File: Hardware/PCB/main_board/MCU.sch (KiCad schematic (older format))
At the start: 1 part, among them U2 NUCLEO-F446RE

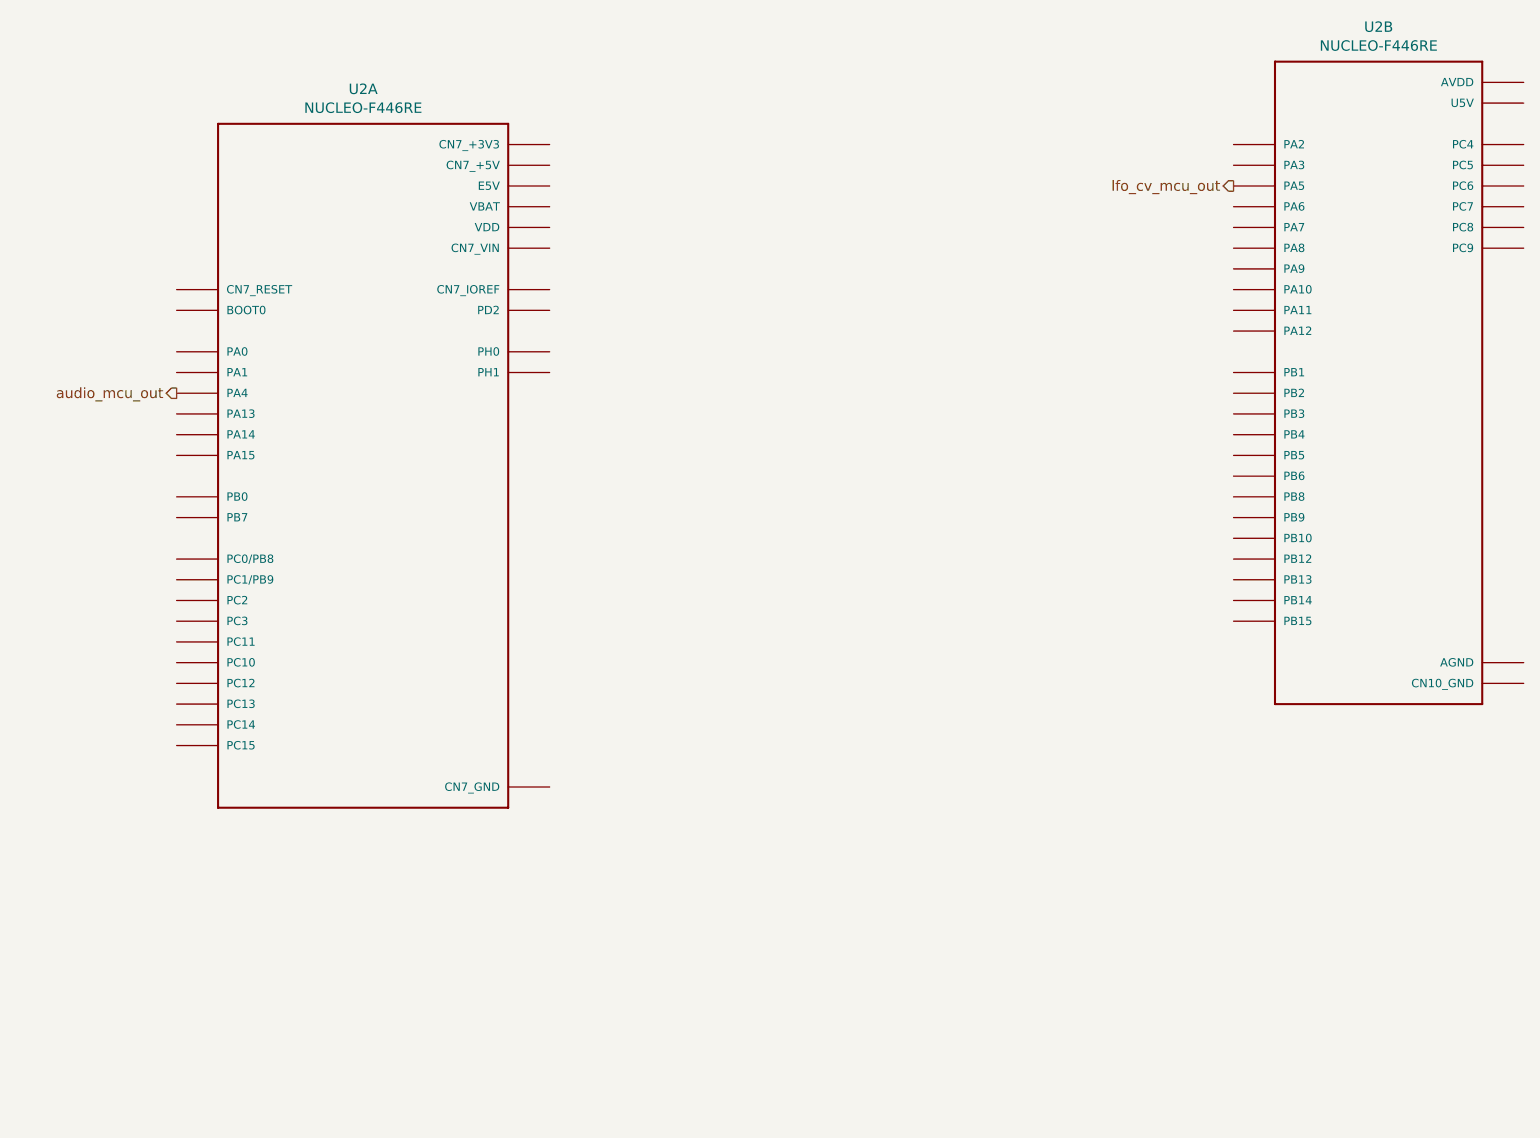
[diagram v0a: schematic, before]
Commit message: Add programming connector to PCB
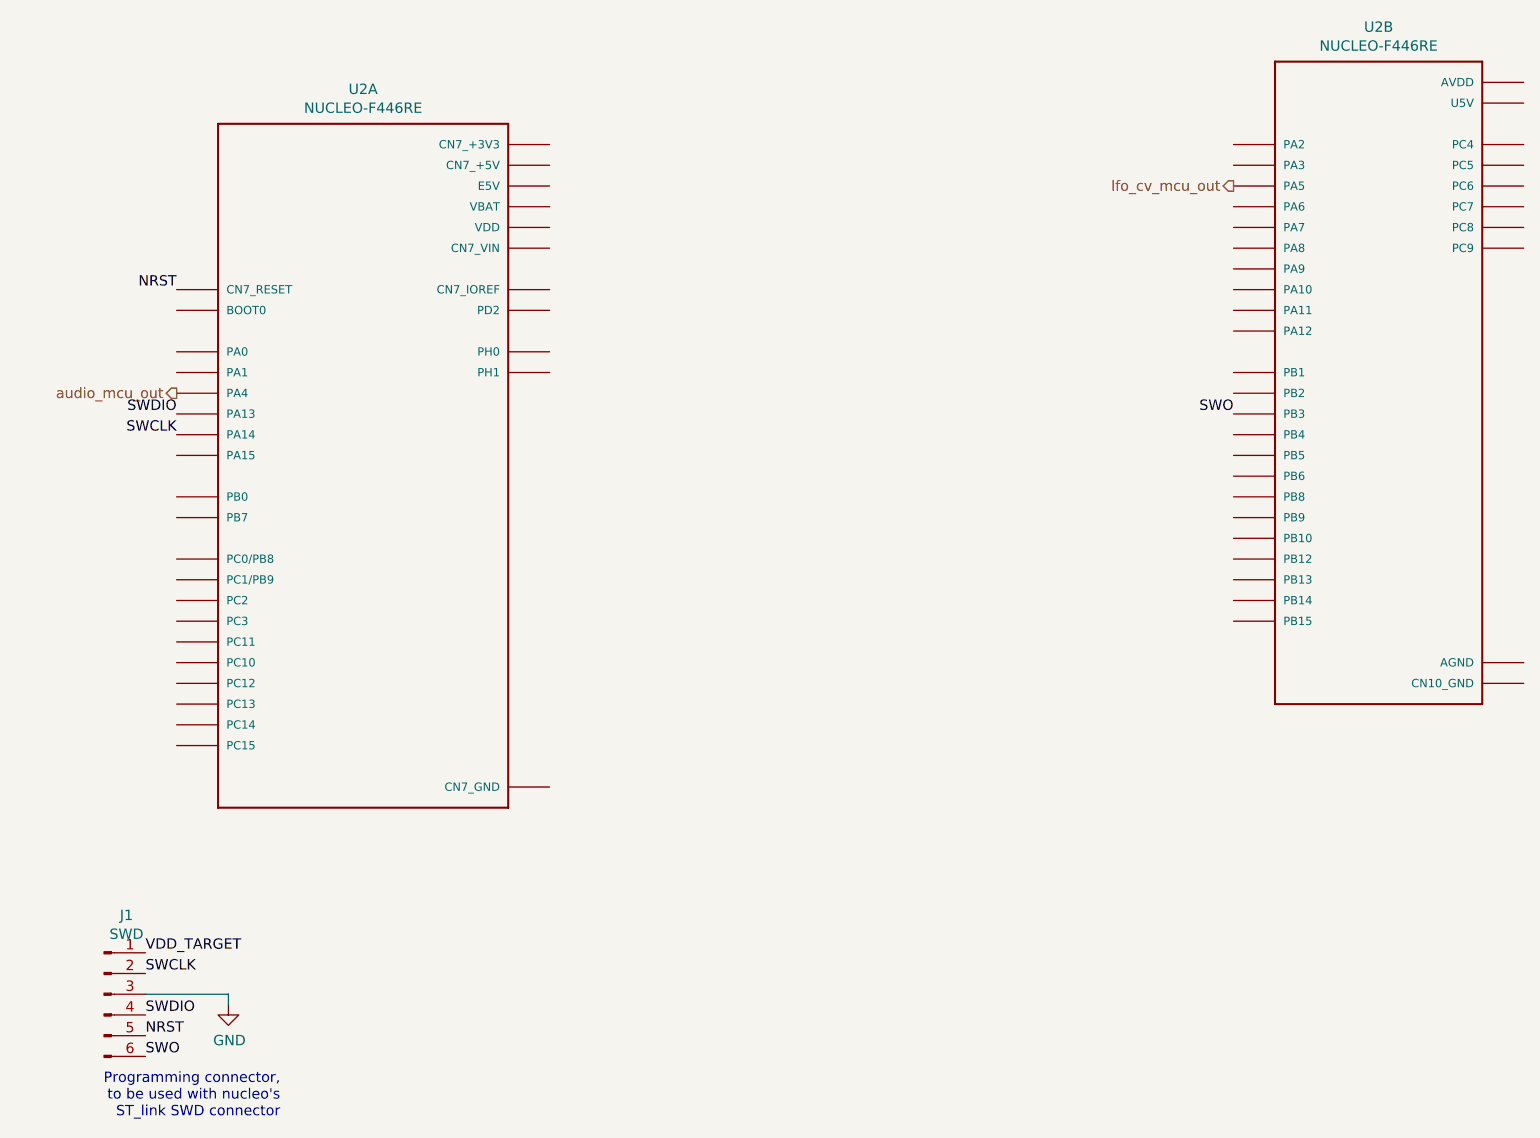
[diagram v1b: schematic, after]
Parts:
- added J1: SWD, Connector_PinHeader_1.27mm:PinHeader_1x06_P1.27mm_Vertical, symbol Connector:Conn_01x06_Male
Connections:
- net SWDIO: now reaches U2.CN7_13 (PA13)
- net SWDIO: now also J1.4 (Pin_4)
- net NRST: now reaches U2.CN7_14 (CN7_RESET)
- net NRST: now also J1.5 (Pin_5)
- net SWCLK: now reaches U2.CN7_15 (PA14)
- net SWCLK: now also J1.2 (Pin_2)
- net SWO: now reaches U2.CN10_31 (PB3)
- net SWO: now also J1.6 (Pin_6)
- new net GND: J1.3 (Pin_3)
- new net VDD_TARGET: J1.1 (Pin_1)
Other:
- note added: "Programming connector,\nto be used with nucleo's\nST_link SWD connector"
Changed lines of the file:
@@
 Text HLabel 7650 2250 0    50   Output ~ 0
 lfo_cv_mcu_out
+$Comp
+L Connector:Conn_01x06_Male J1
+U 1 1 5E51B937
+P 2200 6150
+F 0 "J1" H 2308 6531 50  0000 C CNN
+F 1 "SWD" H 2308 6440 50  0000 C CNN
+F 2 "Connector_PinHeader_1.27mm:PinHeader_1x06_P1.27mm_Vertical" H 2200 6150 50  0001 C CNN
+F 3 "~" H 2200 6150 50  0001 C CNN
+	1    2200 6150
+	1    0    0    -1
+$EndComp
+Text Label 2400 5950 0    50   ~ 0
+VDD_TARGET
+Text Label 2400 6050 0    50   ~ 0
+SWCLK
+Text Label 2400 6250 0    50   ~ 0
+SWDIO
+Text Label 2400 6350 0    50   ~ 0
+NRST
+Text Label 2400 6450 0    50   ~ 0
+SWO
+$Comp
+L power:GND #PWR0102
+U 1 1 5E51E3F2
+P 2800 6200
+F 0 "#PWR0102" H 2800 5950 50  0001 C CNN
+F 1 "GND" H 2805 6027 50  0000 C CNN
+F 2 "" H 2800 6200 50  0001 C CNN
+F 3 "" H 2800 6200 50  0001 C CNN
+	1    2800 6200
+	1    0    0    -1
+$EndComp
+Wire Wire Line
+	2400 6150 2800 6150
+Wire Wire Line
+	2800 6150 2800 6200
+Text Label 2550 3450 2    50   ~ 0
+SWCLK
+Text Label 2550 3350 2    50   ~ 0
+SWDIO
+Text Label 2550 2750 2    50   ~ 0
+NRST
+Text Label 7650 3350 2    50   ~ 0
+SWO
+Text Notes 3050 6750 2    50   ~ 0
+Programming connector,\nto be used with nucleo's\nST_link SWD connector
 $EndSCHEMATC

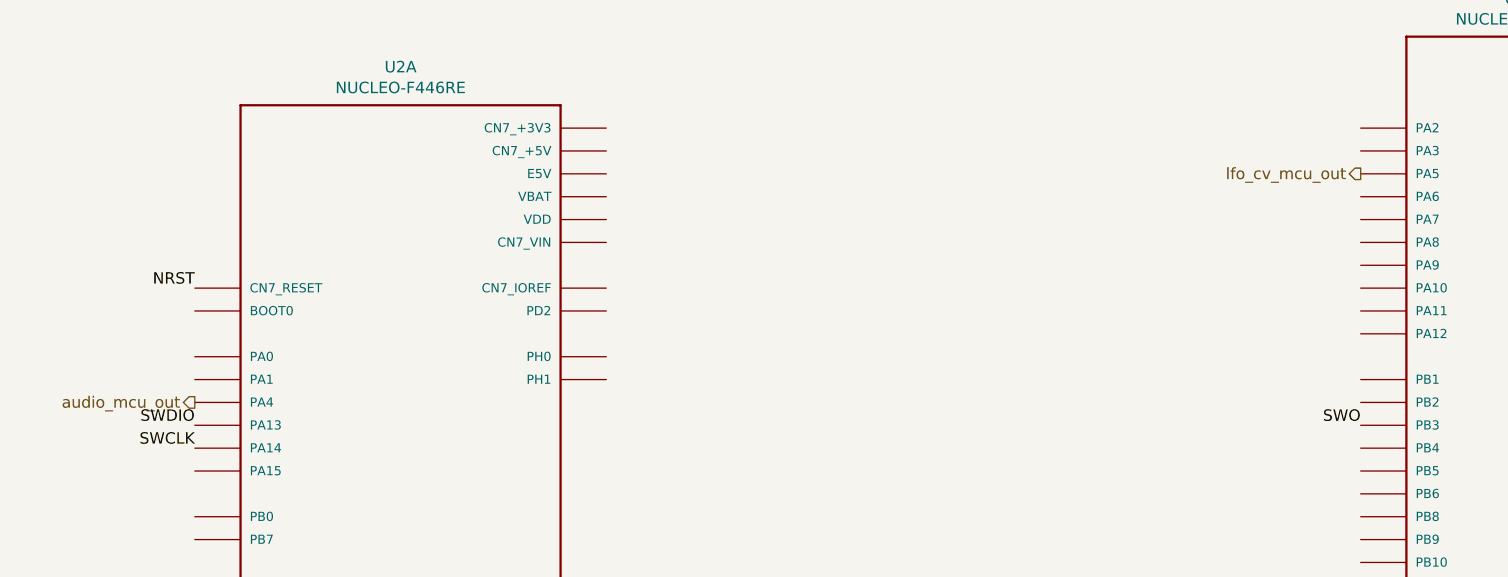
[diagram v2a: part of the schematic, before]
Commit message: Add power supply schematics and layout
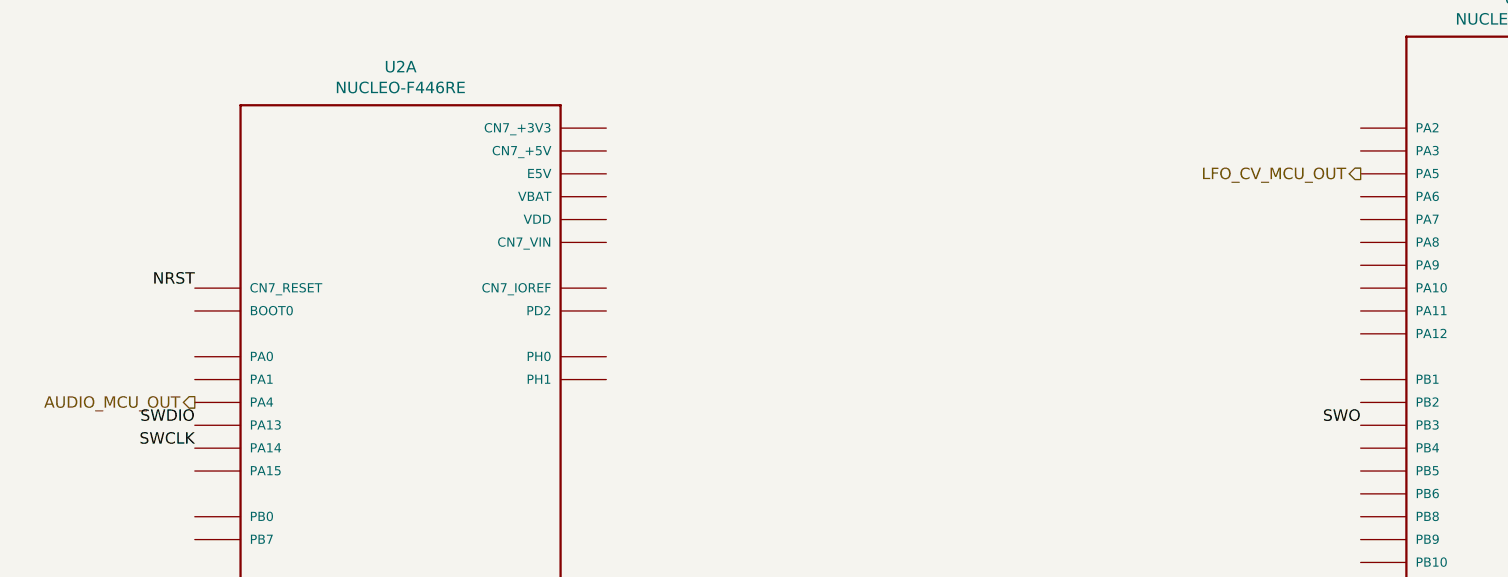
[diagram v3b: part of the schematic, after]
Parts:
- U2: footprint MODULE_NUCLEO-F446RE -> lib:MODULE_NUCLEO-F446RE
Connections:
- net audio_mcu_out renamed AUDIO_MCU_OUT
- net lfo_cv_mcu_out renamed LFO_CV_MCU_OUT
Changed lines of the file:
@@
 $Descr A4 11693 8268
 encoding utf-8
-Sheet 3 4
+Sheet 4 5
 Title ""
 Date ""
@@
 F 0 "U2" H 3450 5317 50  0000 C CNN
 F 1 "NUCLEO-F446RE" H 3450 5226 50  0000 C CNN
-F 2 "MODULE_NUCLEO-F446RE" H 3450 3550 50  0001 L BNN
+F 2 "lib:MODULE_NUCLEO-F446RE" H 3450 3550 50  0001 L BNN
 F 3 "" H 3450 3550 50  0001 L BNN
 F 4 "STMicroelectronics" H 3450 3550 50  0001 L BNN "Champ4"
@@
 F 0 "U2" H 8350 4817 50  0000 C CNN
 F 1 "NUCLEO-F446RE" H 8350 4726 50  0000 C CNN
-F 2 "MODULE_NUCLEO-F446RE" H 8350 3150 50  0001 L BNN
+F 2 "lib:MODULE_NUCLEO-F446RE" H 8350 3150 50  0001 L BNN
 F 3 "" H 8350 3150 50  0001 L BNN
 F 4 "STMicroelectronics" H 8350 3150 50  0001 L BNN "Champ4"
@@
 $EndComp
 Text HLabel 2550 3250 0    50   Output ~ 0
-audio_mcu_out
+AUDIO_MCU_OUT
 Text HLabel 7650 2250 0    50   Output ~ 0
-lfo_cv_mcu_out
+LFO_CV_MCU_OUT
 $Comp
 L Connector:Conn_01x06_Male J1

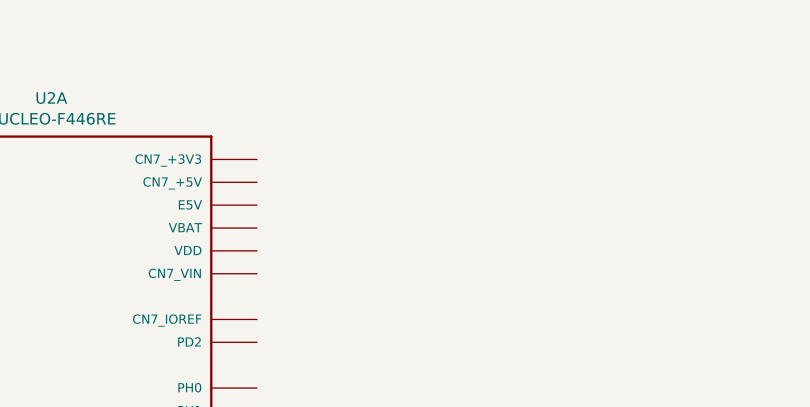
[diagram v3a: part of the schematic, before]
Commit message: Add missing power connection
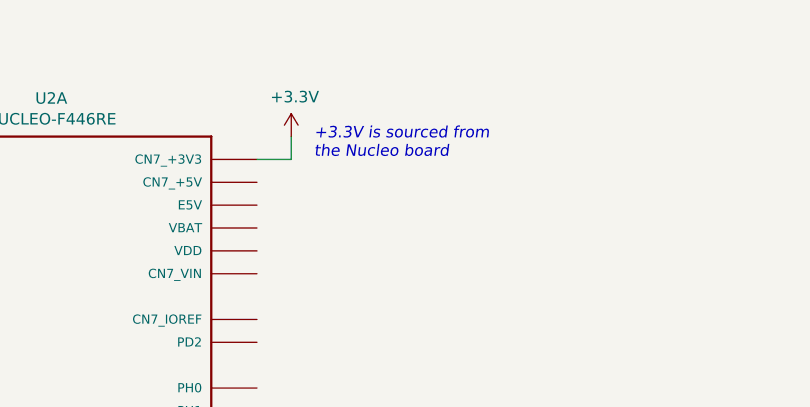
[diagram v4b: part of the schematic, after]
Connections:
- net +3V3: now reaches U2.CN7_16 (CN7_+3V3)
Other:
- note added: "+3.3V is sourced from\nthe Nucleo board"
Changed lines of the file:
@@
 Text Notes 3050 6750 2    50   ~ 0
 Programming connector,\nto be used with nucleo's\nST_link SWD connector
+$Comp
+L power:+3.3V #PWR?
+U 1 1 5E519977
+P 4500 1950
+F 0 "#PWR?" H 4500 1800 50  0001 C CNN
+F 1 "+3.3V" H 4515 2123 50  0000 C CNN
+F 2 "" H 4500 1950 50  0001 C CNN
+F 3 "" H 4500 1950 50  0001 C CNN
+	1    4500 1950
+	1    0    0    -1
+$EndComp
+Wire Wire Line
+	4350 2050 4500 2050
+Wire Wire Line
+	4500 2050 4500 1950
+Text Notes 4600 2050 0    50   Italic 0
++3.3V is sourced from\nthe Nucleo board
 $EndSCHEMATC

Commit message: Flip connectors, add 3D models
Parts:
- J1: footprint Connector_PinHeader_1.27mm:PinHeader_1x06_P1.27mm_Vertical -> Connector_PinHeader_2.54mm:PinHeader_1x06_P2.54mm_Vertical
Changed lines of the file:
@@
 F 0 "J1" H 2308 6531 50  0000 C CNN
 F 1 "SWD" H 2308 6440 50  0000 C CNN
-F 2 "Connector_PinHeader_1.27mm:PinHeader_1x06_P1.27mm_Vertical" H 2200 6150 50  0001 C CNN
+F 2 "Connector_PinHeader_2.54mm:PinHeader_1x06_P2.54mm_Vertical" H 2200 6150 50  0001 C CNN
 F 3 "~" H 2200 6150 50  0001 C CNN
 	1    2200 6150
